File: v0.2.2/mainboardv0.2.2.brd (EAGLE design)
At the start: 33.3 x 29.2 mm, 17 parts, among them U1 BC127, Y1 MHz

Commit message: Begin the routing
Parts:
- removed U2: (no value), SparkFun-PowerIC:SOT23-5
- moved R5 36.2 mm to (41.5, 12.8)
- moved R4 30.2 mm to (43.2, 18.2)
- moved JP1 21.1 mm to (19.1, 1.65), turned to 0 degrees
- moved U1 18.4 mm to (10.2, 28.3), turned to 270 degrees
- moved R1 18.2 mm to (28.4, 12.2), turned to 135 degrees
- moved C3 16.7 mm to (23.7, 8.51), turned to 315 degrees
- moved Y1 15.7 mm to (3.94, 13.5)
- moved R3 15.1 mm to (20.4, 6.22), turned to 180 degrees
- moved C1 15.0 mm to (7.11, 10.8)
- moved S1 14.2 mm to (17.8, 14.4)
- moved R2 13.4 mm to (17.4, 6.22), turned to 180 degrees
- moved D1 13.0 mm to (24.4, 26.4)
- moved C2 11.2 mm to (3.30, 9.78)
- moved TP2 11.1 mm to (9.40, 21.0), flipped to the top
- moved TP1 10.0 mm to (10.2, 20.8), flipped to the top
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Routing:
- net +3V3: track 17.0 -> 0.00 mm, vias 1 -> 0
- net LED: track 16.2 -> 0.00 mm
- net N$9: track 9.06 -> 0.00 mm, vias 1 -> 0
- net VCC/2: track 12.7 -> 20.6 mm
- net N$3: track 7.02 -> 0.00 mm
- net N$1: track 5.03 -> 0.00 mm
- net N$2: track 4.61 -> 0.00 mm
- net N$4: track 3.10 -> 6.98 mm
- net N$6: track 2.08 -> 0.00 mm
- net D+: track 3.19 -> 5.23 mm
- net N$5: track 1.91 -> 0.00 mm
- net N$8: track 2.27 -> 3.93 mm
- net N$7: track 2.52 -> 1.98 mm
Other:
- board size 33.3 x 29.2 mm -> 36.8 x 35.3 mm
- board text removed: "2014 ArchimedesPi / Liam M."
- board text removed: "21-J14-AP-MR-EG"
- board text removed: "HH v2.1dev"

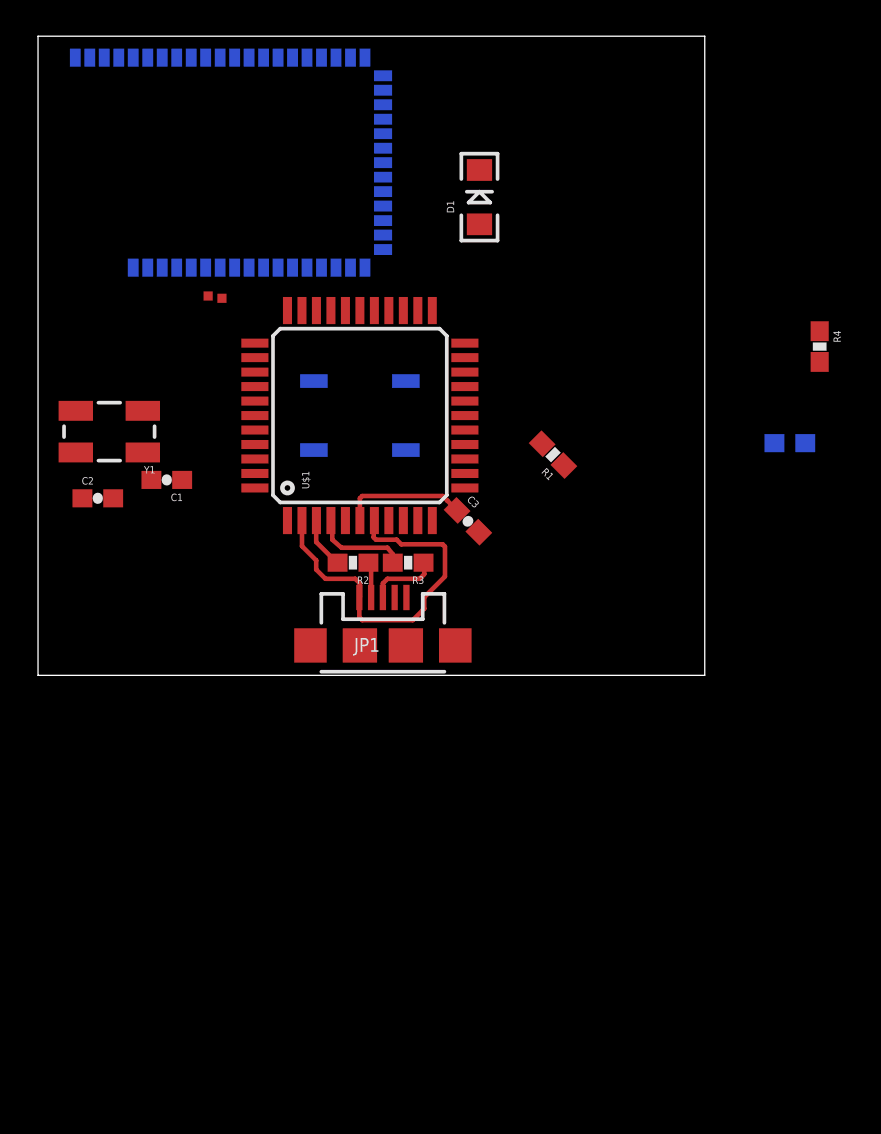
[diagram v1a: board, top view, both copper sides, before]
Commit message: Routed the button and LED
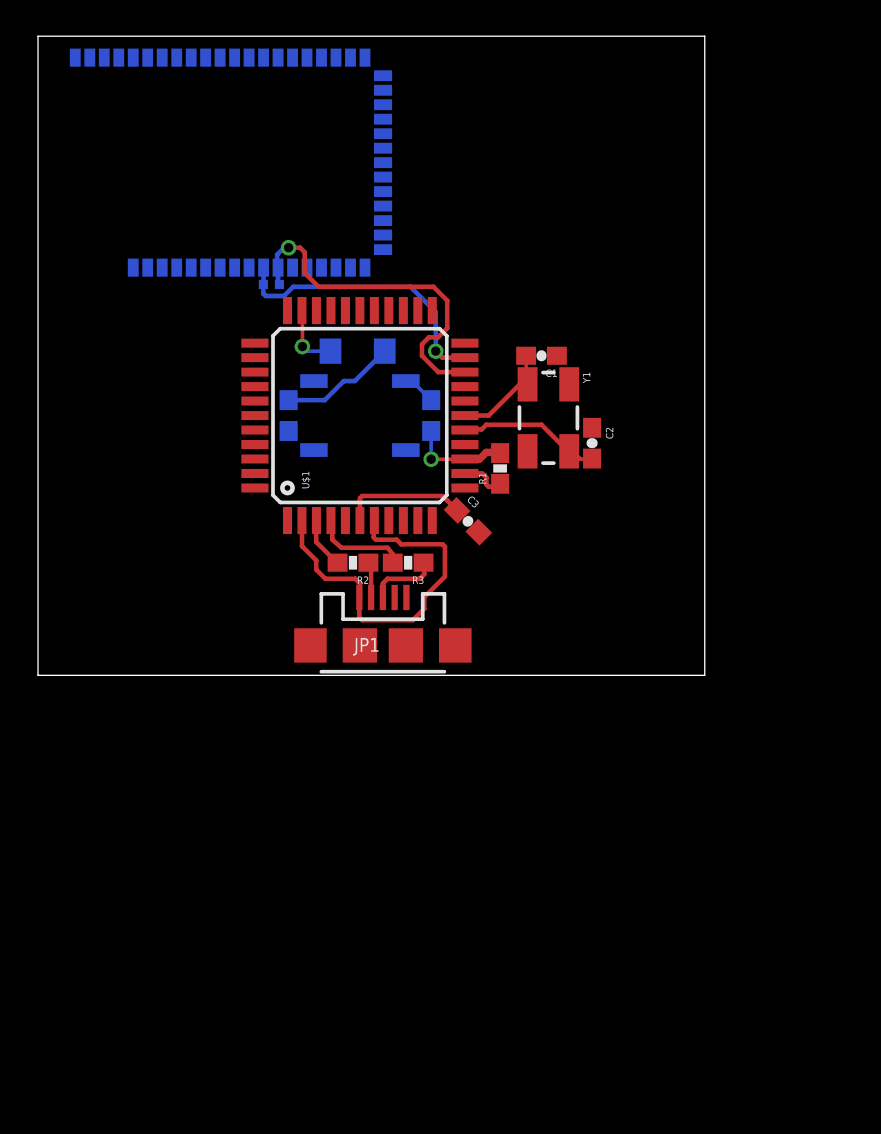
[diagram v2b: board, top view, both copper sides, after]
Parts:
- moved R4 29.6 mm to (13.8, 14.4), flipped to the bottom
- moved C2 27.5 mm to (30.6, 12.8), turned to 270 degrees
- moved Y1 24.3 mm to (28.2, 14.2), turned to 270 degrees
- moved C1 21.8 mm to (27.8, 17.7)
- moved R5 19.9 mm to (21.7, 14.4), turned to 270 degrees
- moved D1 10.8 mm to (17.7, 17.9), flipped to the bottom, turned to 180 degrees
- moved TP2 3.99 mm to (13.3, 21.6), flipped to the bottom
- moved R1 3.02 mm to (25.5, 11.4), turned to 90 degrees
- moved TP1 2.41 mm to (12.4, 21.6), flipped to the bottom
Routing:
- net N$9: track 0.00 -> 19.8 mm, vias 0 -> 1
- net N$10: track 0.00 -> 15.7 mm, vias 0 -> 1
- net N$3: track 0.00 -> 7.95 mm
- net N$5: track 0.00 -> 6.43 mm
- net N$2: track 0.00 -> 5.79 mm
- net +3V3: track 0.00 -> 5.55 mm, vias 0 -> 1
- net LED: track 0.00 -> 3.65 mm, vias 0 -> 1
- net N$1: track 0.00 -> 2.54 mm
- net N$6: track 0.00 -> 1.83 mm

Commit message: More routing
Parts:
- added C10, C5: 180pF, SparkFun-Capacitors:0603-CAP
- added C11, C13, C6, C8: 0.1uF, SparkFun-Capacitors:0603-CAP
- added C12, C14, C7, C9: 47pF, SparkFun-Capacitors:0603-CAP
- added C15, C16, C17: 1.0uF, SparkFun-Capacitors:0603-CAP
- added R13, R16, R19, R22: 15K, SparkFun-Resistors:0603-RES
- added R14, R18, R20, R24: 30.1k, SparkFun-Resistors:0603-RES
- added R15, R17, R21, R23: 43k, SparkFun-Resistors:0603-RES
- added R27: 10K, SparkFun-Resistors:0603-RES
- added U3: TPA6138A2, SparkFun-AnalogIC:TSSOP-14
- moved C1 0.13 mm to (27.8, 17.8)
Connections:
- new net 3.3V: C17.1, R27.1, U3.9
- new net L_OUT: C9.1, R18.1, U3.3
- new net N$11: C8.2, R16.2
- new net N$12: C6.2, R13.2
- new net N$13: C5.1, R13.1, R15.2, R18.2
- new net N$14: C9.2, R15.1, U3.2
- new net N$15: C7.1, R17.1, U3.1
- new net N$16: C5.2, R14.1, R16.1, R17.2
- new net N$17: C10.1, R19.1, R20.2, R21.2
- new net N$18: C12.2, R21.1, U3.14
- new net N$19: C11.2, R19.2
- new net N$20: C10.2, R22.1, R23.2, R24.2
- new net N$21: C13.2, R22.2
- new net N$22: C14.2, R23.1, U3.13
- new net N$23: R27.2, U3.5
- new net N$24: C16.1, U3.6
- new net N$25: C15.2, U3.7
- new net N$26: C15.1, U3.8
- new net R_OUT: C14.1, R24.1, U3.12
- new net SPKR_LN: C6.1, U1.13
- new net SPKR_LP: C8.1, U1.14
- new net SPKR_RN: C13.1, U1.15
- new net SPKR_RP: C11.1, U1.16
- net GND: now also C12.1, C16.2, C17.2, C7.2, R14.2, R20.1, U3.10, U3.4
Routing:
- net +3V3: track 5.55 -> 13.2 mm, vias 1 -> 2
